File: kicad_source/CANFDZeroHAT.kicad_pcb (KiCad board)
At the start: 2 copper layers, 65 x 30 mm, 24 parts, among them CN1 RASPI-IO, CN2 691322310004, CN3 GH_SM04B-GHS-TB, CN4 GH_SM04B-GHS-TB, SW1 JS202011JCQN, U1 MCP2518FD, U2 TCAN332GDR, Y1 RH100-20.000-20-3030-TR

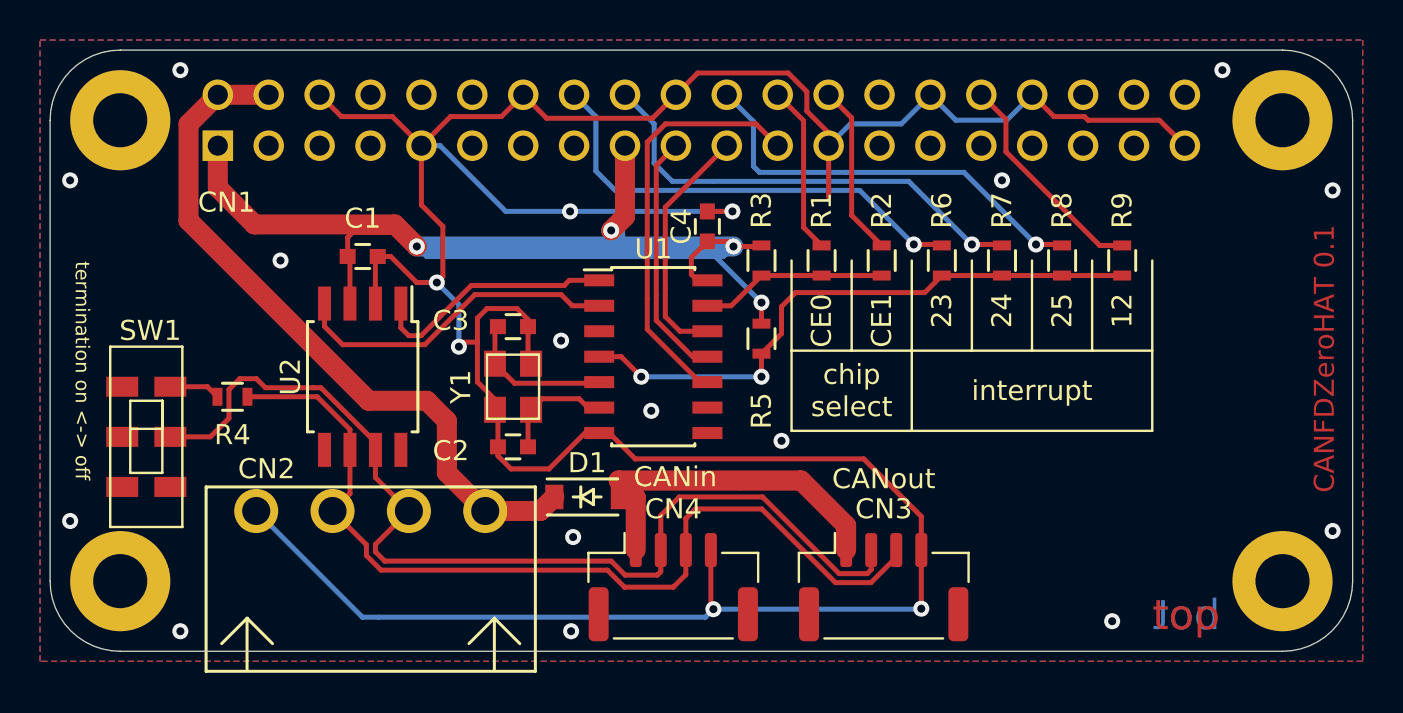
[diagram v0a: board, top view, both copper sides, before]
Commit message: updated layout
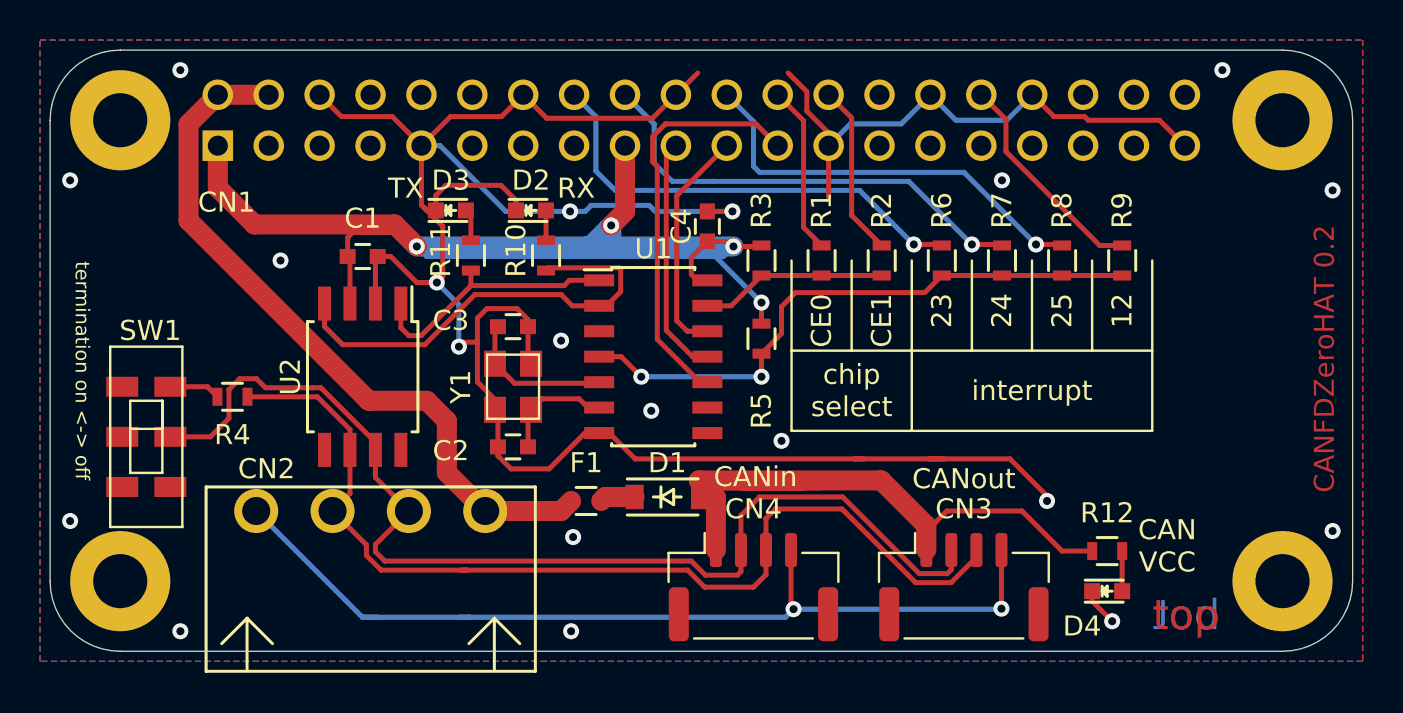
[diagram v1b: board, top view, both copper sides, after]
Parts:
- added D2: 150060GS75000, LEDs:LED_0603, F.Cu at (131.5, 94.5)
- added D3: 150060RS75000, LEDs:LED_0603, F.Cu at (127.5, 94.5)
- added D4: 150060YS75000, LEDs:LED_0603, F.Cu at (160.2, 113.5)
- added F1: 0ZCM0020FF2G, resistors:R_0603, F.Cu at (134.2, 109.0)
- added R10: 1k, resistors:R_0603, F.Cu at (132.2, 96.8)
- added R11: 1k, resistors:R_0603, F.Cu at (128.5, 96.8)
- added R12: 2k, resistors:R_0603, F.Cu at (160.2, 111.5)
- moved CN3 4.00 mm to (153.1, 113.3)
- moved CN4 4.00 mm to (142.6, 113.3)
- moved D1 4.00 mm to (138.3, 108.8)
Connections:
- D1 pad 1: +5V -> /CANVCC_F
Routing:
- net GND: track 170.6 -> 185.6 mm, vias 21 -> 22
- net /CANVCC: track 33.5 -> 43.9 mm
- net /CAN_RX: track 16.5 -> 22.8 mm
- net /CANL: track 45.9 -> 50.2 mm
- net /CANH: track 51.6 -> 55.6 mm
- net Net-(D4-Pad2): track 0.00 -> 2.00 mm
- net /CANVCC_F: track 0.00 -> 1.75 mm
- net +3V3: track 68.8 -> 70.5 mm
- net Net-(D3-Pad2): track 0.00 -> 1.60 mm
- net Net-(D2-Pad2): track 0.00 -> 1.50 mm
- net /CAN_TX: track 12.4 -> 13.2 mm
- net +5V: track 35.5 -> 36.2 mm
- net /SPI_MISO: track 12.2 -> 11.5 mm
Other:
- board text added: "CAN VCC"
- board text added: "CANFDZeroHAT 0.2"
- board text added: "RX"
- board text added: "TX"
- board text removed: "CANFDZeroHAT 0.1"

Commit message: corrected footprint of CAN transceiver
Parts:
- U2: footprint SOIC:SOIJ-8_5.3x5.3mm_Pitch1.27mm -> SOIC:SOIC-8_3.9x4.9mm_Pitch1.27mm
- moved C1 1.10 mm to (123.1, 97.9)
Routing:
- net +3V3: track 70.5 -> 68.3 mm
- net /CAN_TX: track 13.2 -> 12.0 mm
- net GND: track 185.6 -> 186.8 mm
- net /CANH: track 55.6 -> 56.5 mm
- net /CANL: track 50.2 -> 50.9 mm
- net +5V: track 36.2 -> 36.8 mm
